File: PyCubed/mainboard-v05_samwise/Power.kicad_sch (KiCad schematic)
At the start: 62 parts, among them J14 Conn_01x06, J19 Conn_01x06, Q2 MBT2222ADW1T1, Q3 MBT2222ADW1T1, U17 BQ25883RGER, U21 TPS7A4501DCQT, U4 ADM1176-1ARMZ-R7, U5 TPS54226PWPR, U6 LT3652HVIMSE#PBF

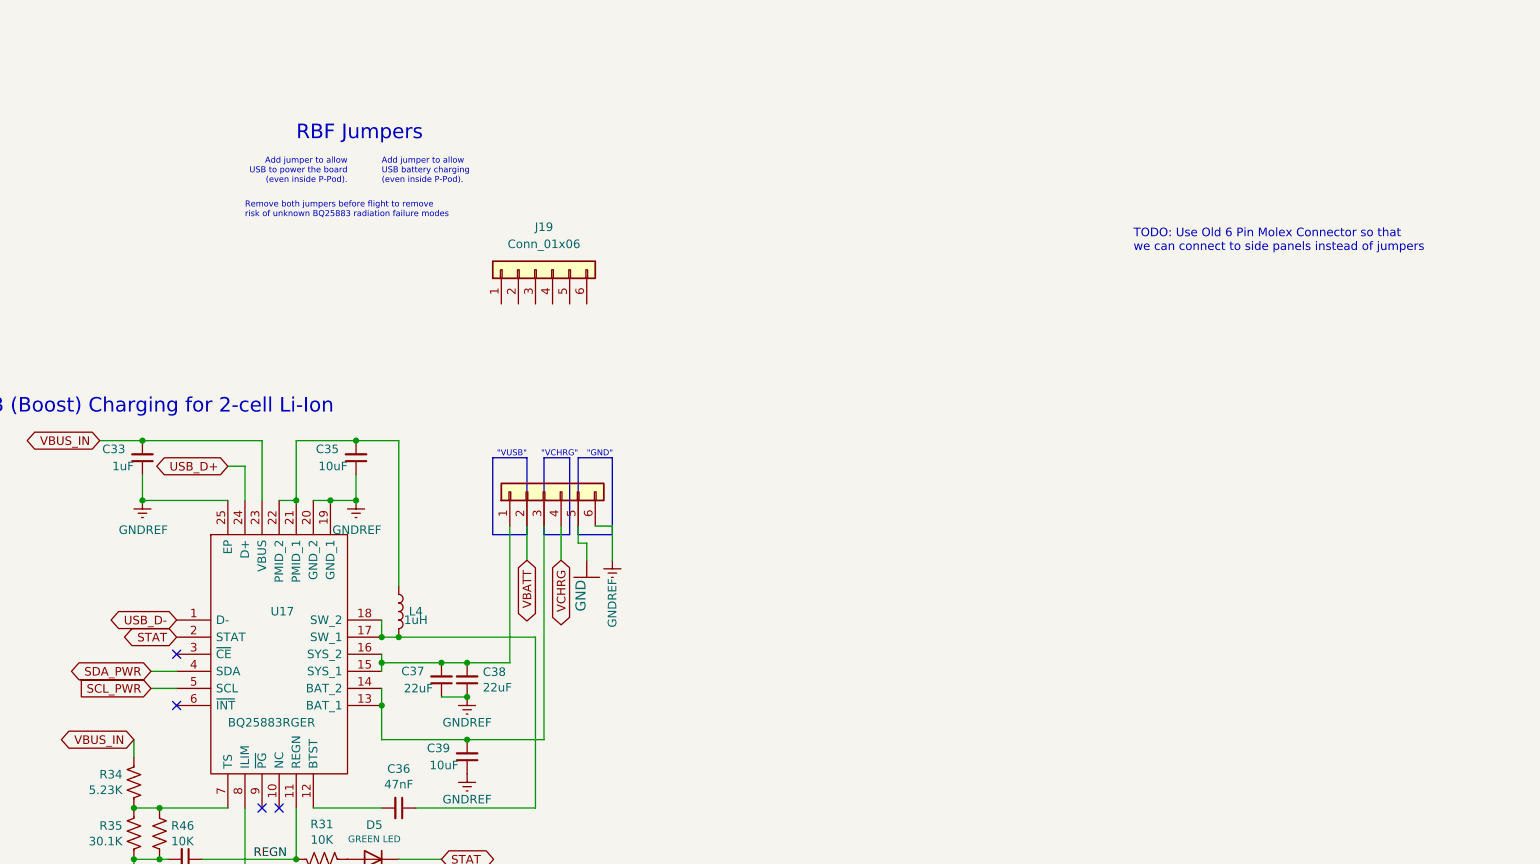
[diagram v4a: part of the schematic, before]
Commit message: added 4 pin side panel connectors
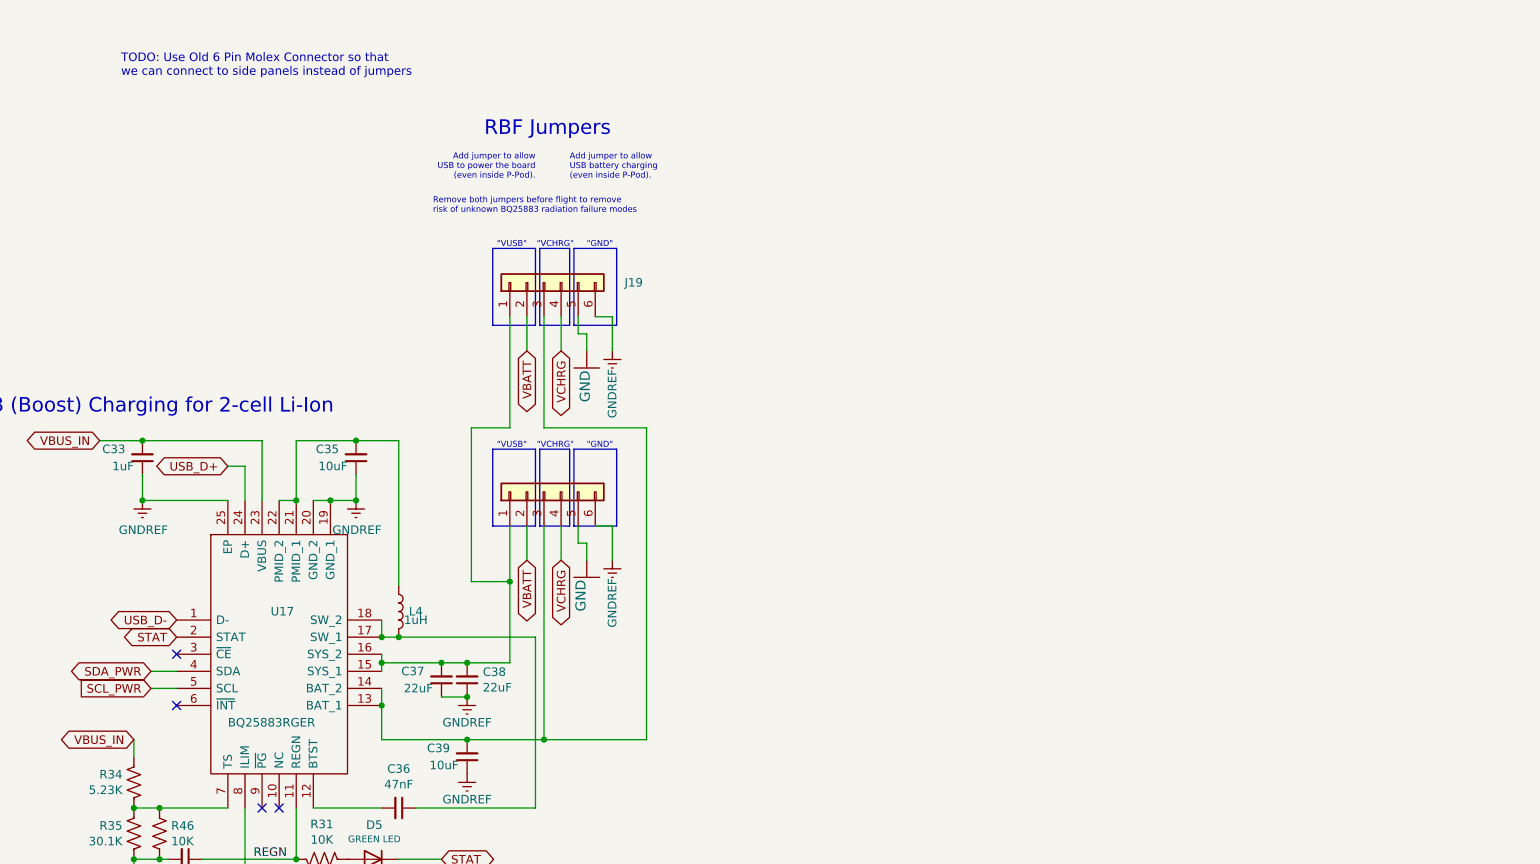
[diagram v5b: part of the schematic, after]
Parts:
- J19: footprint (none) -> mainboard:MOLEX_35362-0650
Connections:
- net GND: now also J19.5 (Pin_5)
- net GNDREF: now also J19.6 (Pin_6)
- net VBATT: now also J19.2 (Pin_2)
- net VCHRG: now also J19.4 (Pin_4)
- net at C37.2, C38.2, J14.1 (Pin_1)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: now also J19.1 (Pin_1)
- net at C39.2, J14.3 (Pin_3), U17.13 (BAT_1)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: now also J19.3 (Pin_3)
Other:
- moved on the sheet: J19

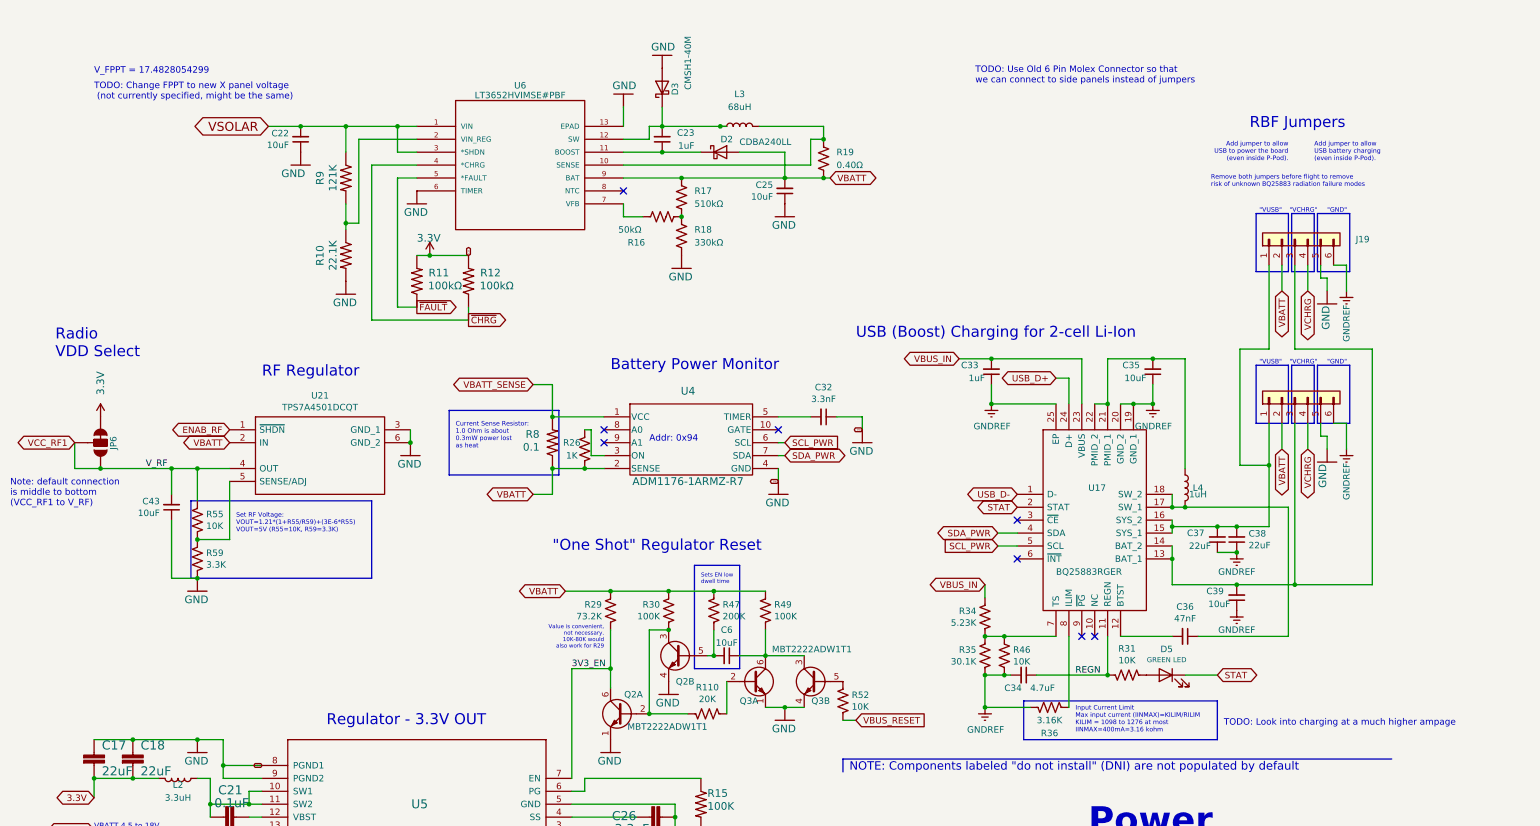
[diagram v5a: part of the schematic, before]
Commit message: schematic changes to power
Added MPPT power module
Increased USB charging input current limit
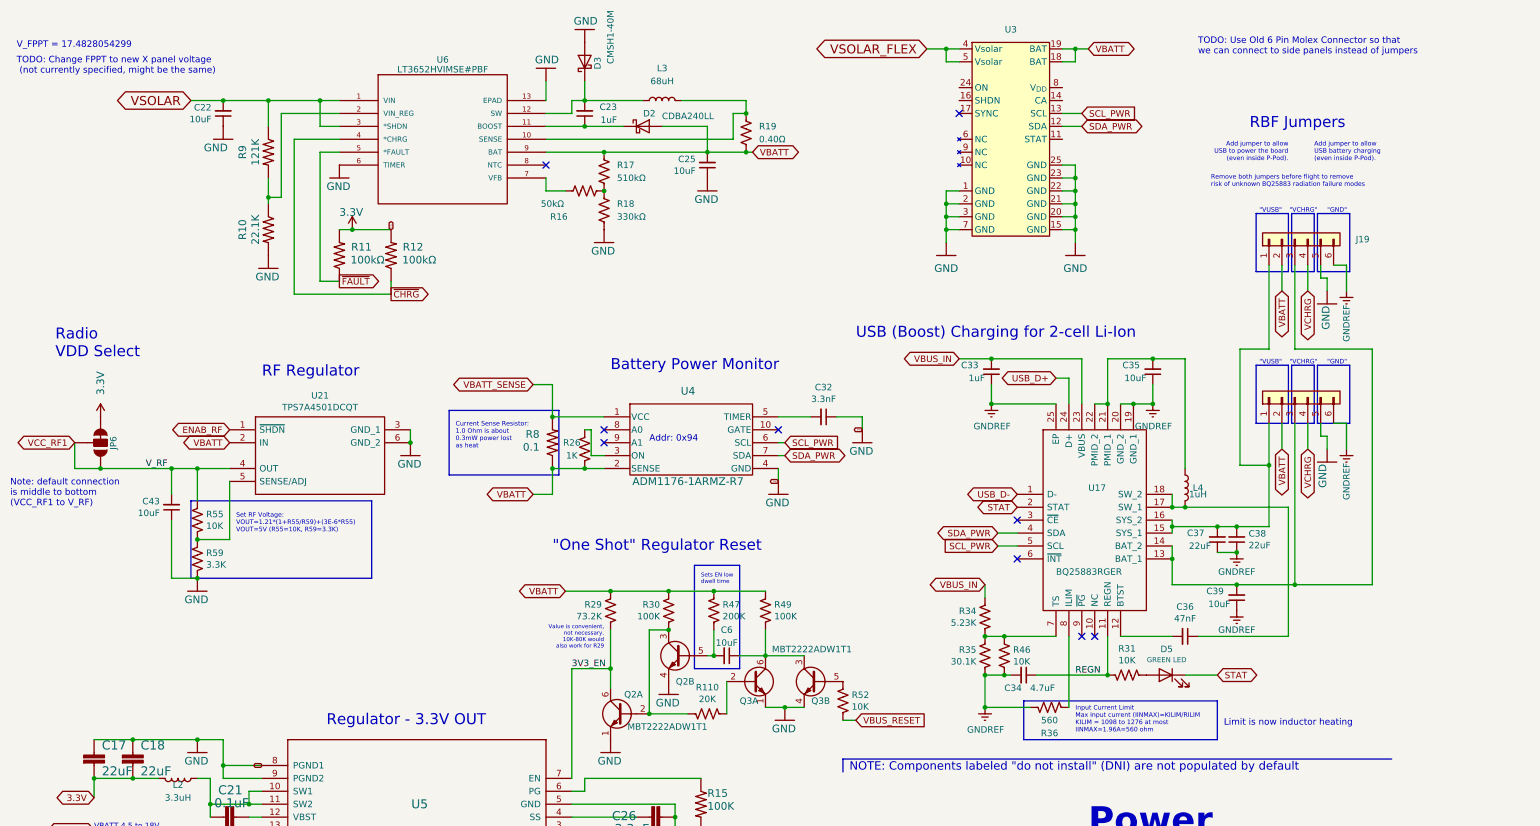
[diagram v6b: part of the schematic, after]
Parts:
- added U3: ~, symbol mainboard:MPPT_module
- R36: value 3.16K -> 560
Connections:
- net GND: now also U3.1 (GND), U3.15 (GND), U3.2 (GND), U3.20 (GND), U3.21 (GND), U3.22 (GND), U3.23 (GND), U3.25 (GND), U3.3 (GND), U3.7 (GND)
- net SCL_PWR: now also U3.13 (SCL)
- net SDA_PWR: now also U3.12 (SDA)
- net VBATT: now also U3.18 (BAT), U3.19 (BAT)
- new net VSOLAR_FLEX: U3.4 (Vsolar), U3.5 (Vsolar)
- no-connect marks 8 -> 9
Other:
- note added: "Input Current Limit Max input current (IINMAX)=KILIM/RILIM KILIM = 1098 to 1276 at most IINMAX=1.96A=560 ohm"
- note added: "Limit is now inductor heating"
- note removed: "Input Current Limit Max input current (IINMAX)=KILIM/RILIM KILIM = 1098 to 1276 at most IINMAX=400mA=3.16 kohm"
- note removed: "TODO: Look into charging at a much higher ampage"
- moved on the sheet: C22, C23, C25, D2, D3, L3, R10, R11, R12, R16, R17, R18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

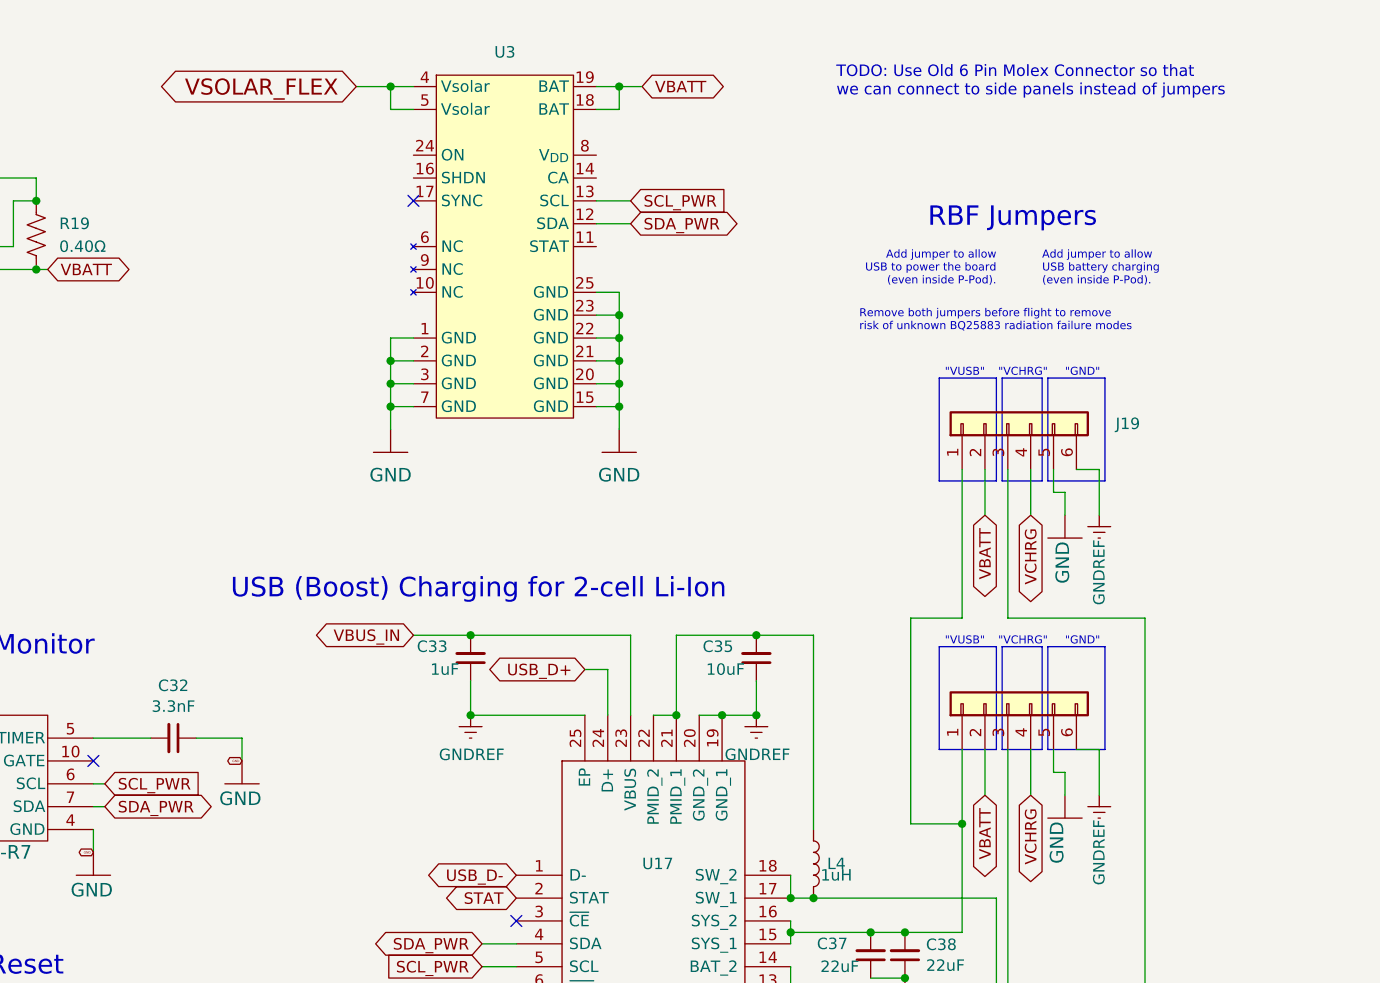
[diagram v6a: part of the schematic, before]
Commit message: a bit of schematic cleanup
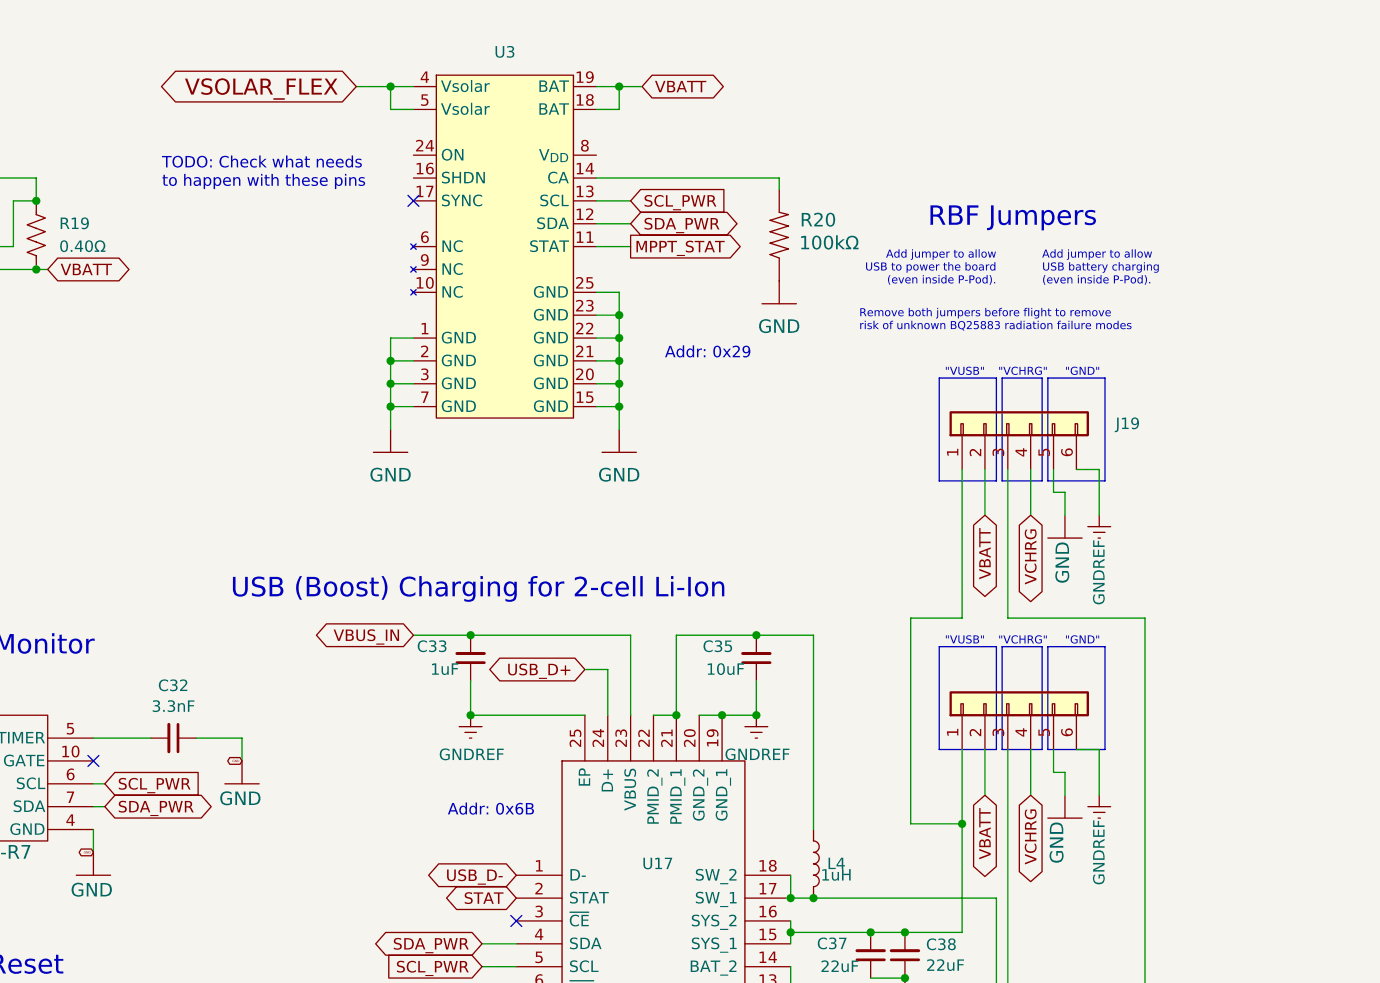
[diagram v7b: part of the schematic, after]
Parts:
- added R20: 100kΩ, Resistor_SMD:R_0603_1608Metric, symbol mainboard:R-US_R0603
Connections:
- net GND: now also R20.1
- net MPPT_STAT: now reaches U3.11 (STAT)
- net at U3.14 (CA): now also R20.2
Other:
- note added: "Addr: 0x29"
- note added: "Addr: 0x6B"
- note added: "TODO: Check what needs to happen with these pins"
- note removed: "TODO: Use Old 6 Pin Molex Connector so that we can connect to side panels instead of jumpers"
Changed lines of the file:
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@@
     (stroke (width 0) (type default))
   )
+  (wire (pts (xy 223.52 40.64) (xy 219.71 40.64))
+    (stroke (width 0) (type default))
+  )
   (wire (pts (xy 168.91 152.4) (xy 165.1 152.4))
     (stroke (width 0) (type default))
@@
     (stroke (width 0) (type default))
   )
+  (wire (pts (xy 240.03 33.02) (xy 240.03 34.29))
+    (stroke (width 0) (type default))
+  )
   (wire (pts (xy 125.73 33.02) (xy 137.16 33.02))
     (stroke (width 0) (type default))
@@
     (stroke (width 0) (type default))
   )
+  (wire (pts (xy 219.71 33.02) (xy 240.03 33.02))
+    (stroke (width 0) (type default))
+  )
   (wire (pts (xy 62.23 163.83) (xy 54.61 163.83))
     (stroke (width 0) (type default))
@@
     (effects (font (size 0.889 0.889)) (justify left bottom))
   )
+  (text "Addr: 0x6B" (at 203.2 104.14 0)
+    (effects (font (size 1.27 1.27)) (justify left bottom))
+  )
   (text "Power" (at 224.79 177.8 0)
     (effects (font (size 5.08 5.08) (thickness 1.016) bold) (justify left bottom))
@@
     (effects (font (size 0.889 0.889)) (justify right bottom))
   )
-  (text "TODO: Use Old 6 Pin Molex Connector so that \nwe can connect to side panels instead of jumpers\n"
-    (at 246.38 24.13 0)
-    (effects (font (size 1.27 1.27) (color 255 0 0 1)) (justify left bottom))
-  )
   (text "Battery Power Monitor" (at 130.81 86.36 0)
     (effects (font (size 2.159 2.159)) (justify left bottom))
@@
     (effects (font (size 1.27 1.27)) (justify left bottom))
   )
+  (text "TODO: Check what needs\nto happen with these pins" (at 171.45 34.29 0)
+    (effects (font (size 1.27 1.27) (color 255 0 0 1)) (justify left bottom))
+  )
+  (text "Addr: 0x29" (at 227.33 53.34 0)
+    (effects (font (size 1.27 1.27)) (justify left bottom))
+  )
   (text "Add jumper to allow\nUSB to power the board\n(even inside P-Pod).\n"
     (at 264.16 45.085 0)
@@
     )
   )
+  (global_label "MPPT_STAT" (shape output) (at 223.52 40.64 0) (fields_autoplaced)
+    (effects (font (size 1.27 1.27)) (justify left))
+    (property "Intersheetrefs" "${INTERSHEET_REFS}" (at 236.0109 40.64 0)
+      (effects (font (size 1.27 1.27)) (justify left) hide)
+    )
+  )
   (global_label "USB_D-" (shape bidirectional) (at 210.82 110.49 180) (fields_autoplaced)
     (effects (font (size 1.27 1.27)) (justify right))
@@
     )
   )
+  (symbol (lib_id "mainboard:R-US_R0603") (at 240.03 39.37 90) (unit 1)
+    (in_bom yes) (on_board yes) (dnp no)
+    (property "Reference" "R20" (at 246.38 36.83 90)
+      (effects (font (size 1.4986 1.4986)) (justify left bottom))
+    )
+    (property "Value" "100kΩ" (at 248.92 39.37 90)
+      (effects (font (size 1.4986 1.4986)) (justify left bottom))
+    )
+    (property "Footprint" "Resistor_SMD:R_0603_1608Metric" (at 240.03 39.37 0)
+      (effects (font (size 1.27 1.27)) hide)
+    )
+    (property "Datasheet" "" (at 240.03 39.37 0)
+      (effects (font (size 1.27 1.27)) hide)
+    )
+    (property "Description" "100K 0603" (at 243.84 38.1 0)
+      (effects (font (size 1.27 1.27)) hide)
+    )
+    (pin "1")
+    (pin "2")
+    (instances
+      (project "mainboard"
+        (path "/db20b18b-d25a-428e-8229-70a189e1de75/00000000-0000-0000-0000-00005cec5dde"
+          (reference "R20") (unit 1)
+        )
+      )
+    )
+  )
   (symbol (lib_id "Device:C_Small") (at 125.73 35.56 180) (unit 1)
     (in_bom yes) (on_board yes) (dnp no)
@@
         )
       )
+    )
+  )
+  (symbol (lib_id "mainboard:GND") (at 240.03 46.99 0) (unit 1)
+    (in_bom yes) (on_board yes) (dnp no) (fields_autoplaced)
+    (property "Reference" "#GND032" (at 240.03 46.99 0)
+      (effects (font (size 1.27 1.27)) hide)
+    )
+    (property "Value" "GND" (at 240.03 49.53 0)
+      (effects (font (size 1.4986 1.4986)))
+    )
+    (property "Footprint" "" (at 240.03 46.99 0)
+      (effects (font (size 1.27 1.27)) hide)
+    )
+    (property "Datasheet" "" (at 240.03 46.99 0)
+      (effects (font (size 1.27 1.27)) hide)
+    )
+    (pin "1")
+    (instances
+      (project "mainboard"
+        (path "/db20b18b-d25a-428e-8229-70a189e1de75/00000000-0000-0000-0000-00005cec5dde"
+          (reference "#GND032") (unit 1)
+        )
+      )
